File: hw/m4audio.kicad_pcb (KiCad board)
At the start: 2 copper layers, 46 x 46 mm, 59 parts, among them J1 JACK_TRS, J2 JACK_TRS, P1 USB_OTG, P2 CONN_01X02, P3 CONN_01X08, P5 CONN_02X05, U1 STM32F405RG, U2 LD1117S33TR, U3 AD8542, U4 WM8731, Y1 Crystal

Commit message: Routing...
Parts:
- added C212: DNP, Capacitors_SMD:C_0805_HandSoldering, B.Cu at (144.0, 132.0)
- added C213: DNP, Capacitors_SMD:C_0805_HandSoldering, B.Cu at (142.0, 132.0)
- added P4: CONN_01X03, Pin_Headers:Pin_Header_Straight_1x03, F.Cu at (147.0, 136.5)
- moved C210 7.50 mm to (156.0, 132.0)
- moved C208 6.00 mm to (151.0, 136.5)
- moved TP1 3.61 mm to (134.0, 98.0)
- moved C211 1.00 mm to (156.0, 125.0)
- moved D1 1.00 mm to (156.0, 130.0)
- moved R12 1.00 mm to (156.0, 128.0)
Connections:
- net +3V3 renamed VDD
- P1 pad 4: (no net) -> /USB_ID
- P5 pad 7: (no net) -> Net-(P5-Pad7)
- P5 pad 8: (no net) -> Net-(P5-Pad8)
- TP2 pad 1: (no net) -> Net-(TP2-Pad1)
- TP201 pad 1: (no net) -> Net-(TP201-Pad1)
- TP202 pad 1: (no net) -> Net-(TP202-Pad1)
- U1 pad 10: (no net) -> Net-(U1-Pad10)
- U1 pad 2: (no net) -> Net-(U1-Pad2)
- U1 pad 22: (no net) -> Net-(U1-Pad22)
- U1 pad 24: (no net) -> Net-(U1-Pad24)
- U1 pad 25: (no net) -> Net-(U1-Pad25)
- U1 pad 26: (no net) -> Net-(U1-Pad26)
- U1 pad 27: (no net) -> Net-(U1-Pad27)
- U1 pad 29: (no net) -> Net-(U1-Pad29)
- U1 pad 3: (no net) -> Net-(U1-Pad3)
- U1 pad 31: (no net) -> Net-(U1-Pad31)
- U1 pad 39: (no net) -> Net-(U1-Pad39)
- U1 pad 4: (no net) -> Net-(U1-Pad4)
- U1 pad 40: (no net) -> Net-(U1-Pad40)
- U1 pad 41: (no net) -> Net-(U1-Pad41)
- U1 pad 42: (no net) -> Net-(U1-Pad42)
- U1 pad 47: (no net) -> Net-(U1-Pad47)
- U1 pad 50: (no net) -> Net-(U1-Pad50)
- U1 pad 51: (no net) -> Net-(U1-Pad51)
- U1 pad 53: (no net) -> Net-(U1-Pad53)
- U1 pad 54: (no net) -> Net-(U1-Pad54)
- U1 pad 56: (no net) -> Net-(U1-Pad56)
- U1 pad 58: (no net) -> Net-(U1-Pad58)
- U1 pad 59: (no net) -> Net-(U1-Pad59)
- U1 pad 61: (no net) -> Net-(U1-Pad61)
- U1 pad 62: (no net) -> Net-(U1-Pad62)
- U4 pad 12: (no net) -> /audio/LINEL
- U4 pad 13: (no net) -> /audio/LINER
- U4 pad 17: (no net) -> Net-(U4-Pad17)
- U4 pad 18: (no net) -> Net-(U4-Pad18)
- U4 pad 2: (no net) -> Net-(U4-Pad2)
- U4 pad 26: (no net) -> Net-(U4-Pad26)
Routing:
- net /audio/ADCLR: track 0.00 -> 25.9 mm, vias 0 -> 2
- net /audio/ADCDAT: track 0.00 -> 22.5 mm, vias 0 -> 2
- net /audio/DACDAT: track 0.00 -> 21.3 mm, vias 0 -> 2
- net /audio/BCLK: track 0.00 -> 18.7 mm, vias 0 -> 2
- net /audio/LINER: track 0.00 -> 7.44 mm, vias 0 -> 1
- net /audio/LINEL: track 0.00 -> 5.49 mm, vias 0 -> 1
- net Net-(C212-Pad2): track 0.00 -> 4.49 mm
- net Net-(C213-Pad2): track 0.00 -> 3.28 mm
- net VDD: track 210.1 -> 213.1 mm, vias 4 -> 10
- net /BOOT1: track 14.6 -> 17.5 mm, vias 2 -> 0
- net GND: track 0.00 -> 2.46 mm, vias 0 -> 1
- net Net-(C210-Pad2): track 5.21 -> 3.60 mm
- net (no net): track 1.50 -> 0.00 mm
- net Net-(R10-Pad2): track 13.6 -> 12.2 mm, vias 2 -> 0
- net /audio/AIN_R: track 5.46 -> 4.62 mm
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- added copper zone on B.Cu, net VDD
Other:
- outline, holes or cut-outs redrawn
- board text added: "1"
- board text added: "2"
- board text added: "3"
- board text added: "3V3"
- board text added: "4"
- board text added: "5"
- board text added: "6"
- board text added: "GND"

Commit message: Routing...
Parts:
- removed TP2: TST, Measurement_Points:Measurement_Point_Square-SMD-Pad_Small
- added OSHW: Symbol_OSHW-Logo_SilkScreen, Symbols:Symbol_OSHW-Logo_SilkScreen, B.Cu at (131.5, 102.5)
- moved TP4 26.4 mm to (140.0, 127.0)
- moved TP3 24.7 mm to (140.0, 122.5)
- moved TP1 11.0 mm to (145.0, 99.0)
- moved C19 1.00 mm to (156.0, 131.0)
- moved D1 1.00 mm to (156.0, 129.0)
- moved R8 1.00 mm to (156.0, 127.0)
- renumbered C3 to C1, C201 to C10, C202 to C11, C203 to C12, C209 to C13, C214 to C14, C215 to C15, C206 to C16, C207 to C17, C208 to C18, C210 to C19, C4 to C2, C211 to C20, C205 to C21, C204 to C22, C212 to C23, C213 to C24, C1 to C3, C2 to C4, C11 to C5, C12 to C6, C14 to C7, C15 to C8, C16 to C9, P2 to P1, P1 to P2, P5 to P3, P3 to P4, P4 to P5, R201 to R10, R202 to R11, R203 to R12, R204 to R13, R205 to R14, R206 to R15, R7 to R2, R8 to R3, R6 to R4, R9 to R5, R10 to R6, R11 to R7, R12 to R8, R13 to R9, TP201 to TP3, TP202 to TP4, U2 to U1, U1 to U2
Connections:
- net VDD renamed +3V3
- TP3 pad 1: Net-(TP201-Pad1) -> /audio/ADCL
- TP4 pad 1: Net-(TP202-Pad1) -> /audio/ADCR
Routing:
- net GND: track 2.46 -> 40.7 mm, vias 1 -> 20
- net /LED1: track 29.1 -> 30.9 mm
- net /audio/bias: track 22.1 -> 23.9 mm
- net /audio/ADCL: track 38.7 -> 40.2 mm
- net /audio/ADCR: track 31.7 -> 33.2 mm
- net Net-(C19-Pad2): track 3.60 -> 4.47 mm
- net /audio/BCLK: track 18.7 -> 19.3 mm
- net Net-(R7-Pad2): track 26.7 -> 26.2 mm
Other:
- outline, holes or cut-outs redrawn
- board text added: "+3.3V"
- board text added: "5-12V"
- board text added: "ARM SWD"
- board text added: "Cortex-M4 DSP board"
- board text added: "Cortex-M4 DSP board rev.A Jonas Norling 2015"
- board text added: "Jonas Norling 2015"
- board text added: "L"
- board text added: "R"
- board text added: "audio in"
- board text added: "headphone"
- board text added: "line out"
- board text added: "rev.A"

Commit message: Add a gnome
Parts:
- added REF**: gnome1, Jonas_Gnomes:gnome1, B.Cu at (130.0, 131.2)
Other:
- board text added: "IN"
- board text added: "OUT"
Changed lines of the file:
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@@
     (area 112.949999 91.949999 159.050001 138.050001)
     (thickness 1.6)
-    (drawings 62)
+    (drawings 64)
     (tracks 687)
     (zones 0)
-    (modules 62)
+    (modules 63)
     (nets 84)
   )
@@
     (fp_line (start 0.35052 -0.89916) (end 0.7493 -1.89992) (layer B.SilkS) (width 0.15))
   )
+  (module Jonas_Gnomes:gnome1 (layer B.Cu)
+    (at 130.005079 131.159904 160)
+    (fp_text reference REF** (at 0 -4 160) (layer B.SilkS) hide
+      (effects (font (size 1 1) (thickness 0.15)) (justify mirror))
+    )
+    (fp_text value gnome1 (at 0.05 6.53 160) (layer B.Fab) hide
+      (effects (font (size 1 1) (thickness 0.15)) (justify mirror))
+    )
+    (fp_line (start 1.96 3.02) (end 2 2.7) (layer B.SilkS) (width 0.15))
+    (fp_line (start 2.45 3.27) (end 2.4 2.83) (layer B.SilkS) (width 0.15))
+    (fp_line (start 2.69 4.74) (end 2.86 4.77) (layer B.SilkS) (width 0.15))
+    (fp_line (start 2.03 5.23) (end 2.2 5.43) (layer B.SilkS) (width 0.15))
+    (fp_line (start 1.36 5.49) (end 1.5 5.79) (layer B.SilkS) (width 0.15))
+    (fp_line (start 0.84 5.4) (end 0.79 5.79) (layer B.SilkS) (width 0.15))
+    (fp_line (start -1.28 3.35) (end -1.6 2.54) (layer B.SilkS) (width 0.15))
+    (fp_line (start -1.63 3.99) (end -2.14 3.18) (layer B.SilkS) (width 0.15))
+    (fp_line (start 0.2 5.29) (end 0.27 5.85) (layer B.SilkS) (width 0.15))
+    (fp_line (start -0.4 5.23) (end -0.52 5.71) (layer B.SilkS) (width 0.15))
+    (fp_line (start -0.91 5.15) (end -1.19 5.59) (layer B.SilkS) (width 0.15))
+    (fp_line (start -1.48 4.43) (end -1.83 4.81) (layer B.SilkS) (width 0.15))
+    (fp_line (start 4.99 -0.2) (end 4.83 0.34) (layer B.SilkS) (width 0.15))
+    (fp_line (start 5.46 -0.25) (end 4.99 -0.2) (layer B.SilkS) (width 0.15))
+    (fp_line (start 5.67 0.29) (end 5.46 -0.25) (layer B.SilkS) (width 0.15))
+    (fp_line (start 5.26 0.57) (end 5.67 0.29) (layer B.SilkS) (width 0.15))
+    (fp_line (start 4.84 0.4) (end 6.32 0.97) (layer B.SilkS) (width 0.15))
+    (fp_line (start 0.92 3.5) (end 0.71 3.47) (layer B.SilkS) (width 0.15))
+    (fp_line (start 0.86 3.98) (end 0.92 3.5) (layer B.SilkS) (width 0.15))
+    (fp_line (start 1.14 3.28) (end 1.16 3.07) (layer B.SilkS) (width 0.15))
+    (fp_line (start 0.77 3.06) (end 0.79 2.95) (layer B.SilkS) (width 0.15))
+    (fp_line (start 0.29 3.05) (end 0.26 2.92) (layer B.SilkS) (width 0.15))
+    (fp_line (start -0.06 3.25) (end -0.13 3.13) (layer B.SilkS) (width 0.15))
+    (fp_line (start 1.39 3.45) (end 1.33 3.41) (layer B.SilkS) (width 0.15))
+    (fp_line (start 0.99 3.18) (end 1.39 3.45) (layer B.SilkS) (width 0.15))
+    (fp_line (start 0.54 2.99) (end 0.99 3.18) (layer B.SilkS) (width 0.15))
+    (fp_line (start -0.33 3.54) (end 0.54 2.99) (layer B.SilkS) (width 0.15))
+    (fp_circle (center -0.02 -1.38) (end 0.04 -1.41) (layer B.Mask) (width 0.15))
+    (fp_circle (center 0.05 -0.57) (end 0.11 -0.62) (layer B.Mask) (width 0.15))
+    (fp_circle (center -0.01 0.47) (end 0.07 0.44) (layer B.Mask) (width 0.15))
+    (fp_circle (center 0.05 1.32) (end 0.13 1.31) (layer B.Mask) (width 0.15))
+    (fp_circle (center 0.11 2.17) (end 0.16 2.12) (layer B.Mask) (width 0.15))
+    (fp_circle (center 1.73 4.19) (end 1.82 4.18) (layer B.Mask) (width 0.15))
+    (fp_circle (center 0.26 4.19) (end 0.33 4.16) (layer B.Mask) (width 0.15))
+    (fp_line (start 1.66 3.81) (end 1.22 4.21) (layer B.SilkS) (width 0.15))
+    (fp_line (start 2.43 3.72) (end 1.66 3.81) (layer B.SilkS) (width 0.15))
+    (fp_line (start 2.25 4.56) (end 2.43 3.72) (layer B.SilkS) (width 0.15))
+    (fp_line (start 1.26 4.19) (end 2.25 4.56) (layer B.SilkS) (width 0.15))
+    (fp_line (start 0.12 3.92) (end -0.59 4.23) (layer B.SilkS) (width 0.15))
+    (fp_line (start 0.7 4.13) (end 0.12 3.92) (layer B.SilkS) (width 0.15))
+    (fp_line (start -0.04 4.66) (end 0.7 4.13) (layer B.SilkS) (width 0.15))
+    (fp_line (start -0.69 4.21) (end -0.04 4.66) (layer B.SilkS) (width 0.15))
+    (fp_line (start 1.73 2.92) (end 0.67 2.6) (layer B.SilkS) (width 0.15))
+    (fp_line (start 2.9 3.54) (end 1.73 2.92) (layer B.SilkS) (width 0.15))
+    (fp_line (start 2.65 4.85) (end 2.9 3.54) (layer B.SilkS) (width 0.15))
+    (fp_line (start 1.44 5.37) (end 2.65 4.85) (layer B.SilkS) (width 0.15))
+    (fp_line (start -0.22 5.18) (end 1.44 5.37) (layer B.SilkS) (width 0.15))
+    (fp_line (start -1.09 4.97) (end -0.22 5.18) (layer B.SilkS) (width 0.15))
+    (fp_line (start -1.62 4.18) (end -1.09 4.97) (layer B.SilkS) (width 0.15))
+    (fp_line (start -1.2 3.1) (end -1.62 4.18) (layer B.SilkS) (width 0.15))
+    (fp_line (start -0.15 2.7) (end -1.2 3.1) (layer B.SilkS) (width 0.15))
+    (fp_line (start -0.11 2.45) (end -0.23 -1.98) (layer B.SilkS) (width 0.15))
+    (fp_line (start 2.11 0.76) (end 4.86 0.39) (layer B.SilkS) (width 0.15))
+    (fp_line (start -3.54 2.19) (end -3.56 2.76) (layer B.SilkS) (width 0.15))
+    (fp_line (start -3.53 2.13) (end -4.3 2.57) (layer B.SilkS) (width 0.15))
+    (fp_line (start -3.48 2.07) (end -4.05 1.81) (layer B.SilkS) (width 0.15))
+    (fp_line (start -1.82 1.02) (end -3.48 2.07) (layer B.SilkS) (width 0.15))
+    (fp_line (start 0.76 -2.99) (end 1.76 -3.06) (layer B.SilkS) (width 0.15))
+    (fp_line (start 0.94 -2.12) (end 0.76 -2.99) (layer B.SilkS) (width 0.15))
+    (fp_line (start -0.71 -2.83) (end -1.41 -2.87) (layer B.SilkS) (width 0.15))
+    (fp_line (start -0.74 -2) (end -0.71 -2.83) (layer B.SilkS) (width 0.15))
+    (fp_line (start 2.06 -2.26) (end -2.02 -1.77) (layer B.SilkS) (width 0.15))
+    (fp_line (start 2.02 0.86) (end 2.06 -2.26) (layer B.SilkS) (width 0.15))
+    (fp_line (start 1.84 2.12) (end 2.02 0.86) (layer B.SilkS) (width 0.15))
+    (fp_line (start 1.22 2.47) (end 1.84 2.12) (layer B.SilkS) (width 0.15))
+    (fp_line (start -0.87 2.61) (end 1.22 2.47) (layer B.SilkS) (width 0.15))
+    (fp_line (start -1.73 1.78) (end -0.87 2.61) (layer B.SilkS) (width 0.15))
+    (fp_line (start -2.08 -1.69) (end -1.73 1.78) (layer B.SilkS) (width 0.15))
+    (pad 1 smd trapezoid (at 0.06 0.15 163) (size 3.6 4.5) (rect_delta 0 -0.4 ) (layers B.Cu))
+  )
+  (gr_text OUT (at 134.5 136.5) (layer B.SilkS)
+    (effects (font (size 1.5 1.5) (thickness 0.3)) (justify mirror))
+  )
+  (gr_text IN (at 123.5 136.5) (layer B.SilkS)
+    (effects (font (size 1.5 1.5) (thickness 0.3)) (justify mirror))
+  )
   (gr_text "Cortex-M4 DSP board" (at 158 112.5 90) (layer F.SilkS)

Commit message: Tuning PCB
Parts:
- moved REF** 0.30 mm to (129.8, 131.0)
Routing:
- net GND: track 40.7 -> 50.1 mm, vias 20 -> 22
- net +3V3: track 212.8 -> 213.7 mm, vias 10 -> 8
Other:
- board text added: "3.3V"
- board text added: "BOOT0"

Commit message: Use only one supply net name, add VCAP on STM32, alternative LED footprints
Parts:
- added C25: 2.2u, Capacitors_SMD:C_0805_HandSoldering, F.Cu at (149.5, 115.5)
- added C26: 2.2u, Capacitors_SMD:C_0805_HandSoldering, F.Cu at (149.0, 102.0)
- added D11: green, LEDs:LED-0805, B.Cu at (156.0, 125.0)
- added D21: orange, LEDs:LED-0805, B.Cu at (128.0, 117.0)
- D1: value LED -> green
- D2: value LED -> orange
- moved C8 2.24 mm to (149.0, 100.0), turned to 0 degrees
- moved C9 1.58 mm to (149.5, 113.5)
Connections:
- net +3V3 renamed VDD
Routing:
- net Net-(D2-Pad2): track 2.12 -> 7.91 mm, vias 0 -> 1
- net GND: track 50.1 -> 55.8 mm, vias 22 -> 23
- net Net-(C25-Pad1): track 0.00 -> 5.33 mm
- net VDD: track 213.7 -> 209.2 mm
- net Net-(C26-Pad1): track 0.00 -> 4.39 mm
- net Net-(D1-Pad2): track 2.12 -> 5.43 mm, vias 0 -> 1
- net Net-(R6-Pad2): track 12.2 -> 13.8 mm

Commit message: Tune PCB design, add protection diode
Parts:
- added D3: SBAT54CLT1G, Housings_SOT-23_SOT-143_TSOT-6:SOT-23_Handsoldering, F.Cu at (153.5, 98.0)
- added J11: CONN_01X03, Pin_Headers:Pin_Header_Straight_1x03, F.Cu at (126.5, 130.0)
- added J21: CONN_01X03, Pin_Headers:Pin_Header_Straight_1x03, F.Cu at (137.5, 130.0)
- moved REF** 12.5 mm to (134.4, 119.4)
- moved P2 2.00 mm to (157.0, 105.0)
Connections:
- P1 pad 2: /PWR_5V -> /9V
- P2 pad 1: /PWR_5V -> /USB_5V
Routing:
- net /USB_5V: track 0.00 -> 11.2 mm
- net /PWR_5V: track 30.3 -> 20.7 mm
- net /9V: track 0.00 -> 4.78 mm
- net /audio/AIN_R: track 4.62 -> 9.04 mm
- net /audio/AOUT_L: track 20.8 -> 24.7 mm
- net /audio/AIN_L: track 14.0 -> 17.8 mm
- net GND: track 55.8 -> 59.0 mm
- net /USB_DM: track 9.13 -> 7.13 mm
- net /audio/AOUT_R: track 41.8 -> 40.3 mm
- net /USB_DP: track 8.17 -> 6.77 mm
- net Net-(R3-Pad2): track 8.03 -> 8.58 mm
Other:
- board text added: "9V"
- board text removed: "5-12V"

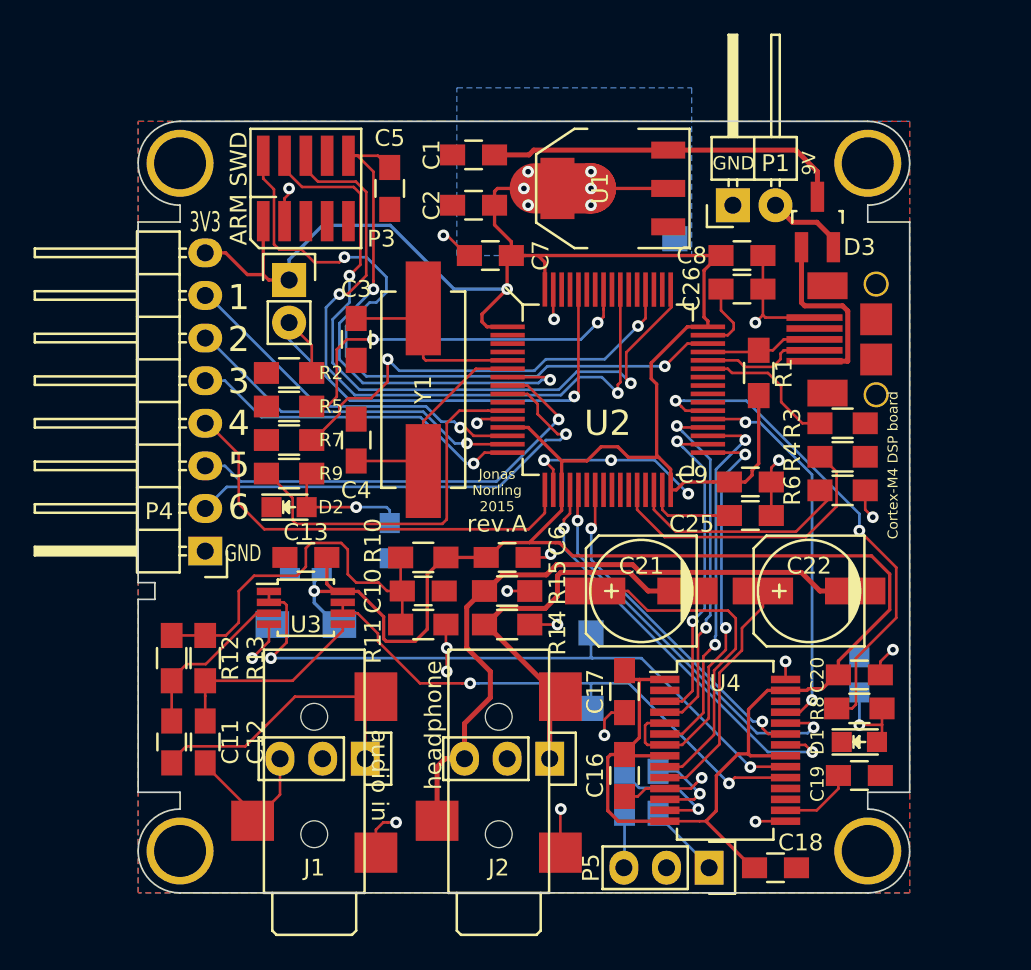
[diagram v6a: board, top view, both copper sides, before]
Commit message: Add I2S test pads
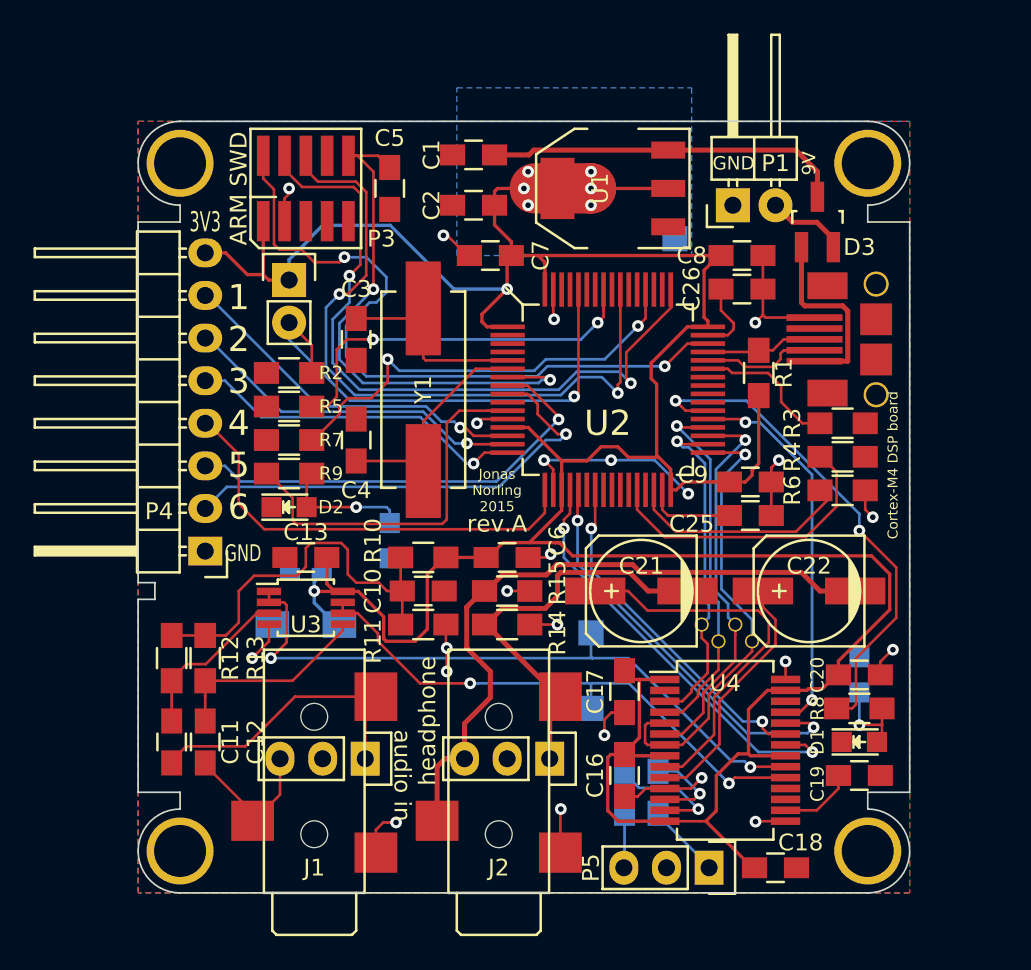
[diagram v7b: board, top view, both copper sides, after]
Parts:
- added TP5: TST, Jonas_Connectors:TP_0.6mm, B.Cu at (147.6, 123.0)
- added TP6: TST, Jonas_Connectors:TP_0.6mm, B.Cu at (149.6, 123.0)
- added TP7: TST, Jonas_Connectors:TP_0.6mm, B.Cu at (148.6, 122.0)
- added TP8: TST, Jonas_Connectors:TP_0.6mm, B.Cu at (146.6, 122.0)
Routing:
- net /audio/DACL: track 20.3 -> 22.9 mm
- net /audio/ADCLR: track 25.9 -> 27.2 mm, vias 2 -> 1
- net /audio/ADCDAT: track 22.5 -> 23.4 mm, vias 2 -> 1
- net /audio/BCLK: track 19.7 -> 20.4 mm, vias 2 -> 1
- net /audio/DACR: track 14.3 -> 14.9 mm
- net /audio/DACDAT: track 21.5 -> 21.9 mm, vias 2 -> 1
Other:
- board text added: "I2S"

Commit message: Standardise on 100k for random stuff
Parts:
- R14, R15: value 47k -> 100k
- R2, R3, R4, R5, R6, R7: value 20k -> 100k
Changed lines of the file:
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@@
   (general
     (links 163)
-    (no_connects 4)
+    (no_connects 0)
     (area 112.949999 91.949999 159.050001 138.050001)
     (thickness 1.6)
@@
       (effects (font (size 1 1) (thickness 0.15)))
     )
-    (fp_text value 20k (at 0 2.1 180) (layer F.Fab)
+    (fp_text value 100k (at 0 2.1 180) (layer F.Fab)
       (effects (font (size 1 1) (thickness 0.15)))
     )
@@
       (effects (font (size 0.8 0.8) (thickness 0.15)))
     )
-    (fp_text value 20k (at 0 2.1) (layer F.Fab)
+    (fp_text value 100k (at 0 2.1) (layer F.Fab)
       (effects (font (size 1 1) (thickness 0.15)))
     )
@@
       (effects (font (size 1 1) (thickness 0.15)))
     )
-    (fp_text value 20k (at 0 2.1 180) (layer F.Fab)
+    (fp_text value 100k (at 0 2.1 180) (layer F.Fab)
       (effects (font (size 1 1) (thickness 0.15)))
     )
@@
       (effects (font (size 0.8 0.8) (thickness 0.15)))
     )
-    (fp_text value 20k (at 0 2.1) (layer F.Fab)
+    (fp_text value 100k (at 0 2.1) (layer F.Fab)
       (effects (font (size 1 1) (thickness 0.15)))
     )
@@
       (effects (font (size 1 1) (thickness 0.15)))
     )
-    (fp_text value 20k (at 0 2.1 180) (layer F.Fab)
+    (fp_text value 100k (at 0 2.1 180) (layer F.Fab)
       (effects (font (size 1 1) (thickness 0.15)))
     )
@@
       (effects (font (size 0.8 0.8) (thickness 0.15)))
     )
-    (fp_text value 20k (at 0 2.1) (layer F.Fab)
+    (fp_text value 100k (at 0 2.1) (layer F.Fab)
       (effects (font (size 1 1) (thickness 0.15)))
     )
@@
       (effects (font (size 1 1) (thickness 0.15)))
     )
-    (fp_text value 47k (at 0 2.1) (layer F.Fab)
+    (fp_text value 100k (at 0 2.1) (layer F.Fab)
       (effects (font (size 1 1) (thickness 0.15)))
     )
@@
       (effects (font (size 1 1) (thickness 0.15)))
     )
-    (fp_text value 47k (at 0 2.1) (layer F.Fab)
-      (effects (font (size 1 1) (thickness 0.15)))
-    )
+    (fp_text value 100k (at 0 2.1) (layer F.Fab)
+      (effects (font (size 1 1) (thickness 0.15)))
+    )
